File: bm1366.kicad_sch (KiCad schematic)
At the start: 47 parts, among them U12 BM1366_mode1, U5 MCP1824T-1202E/OT, U6 MCP1824T-0802E, U7 25MHz, U9 SN74AVC4T774

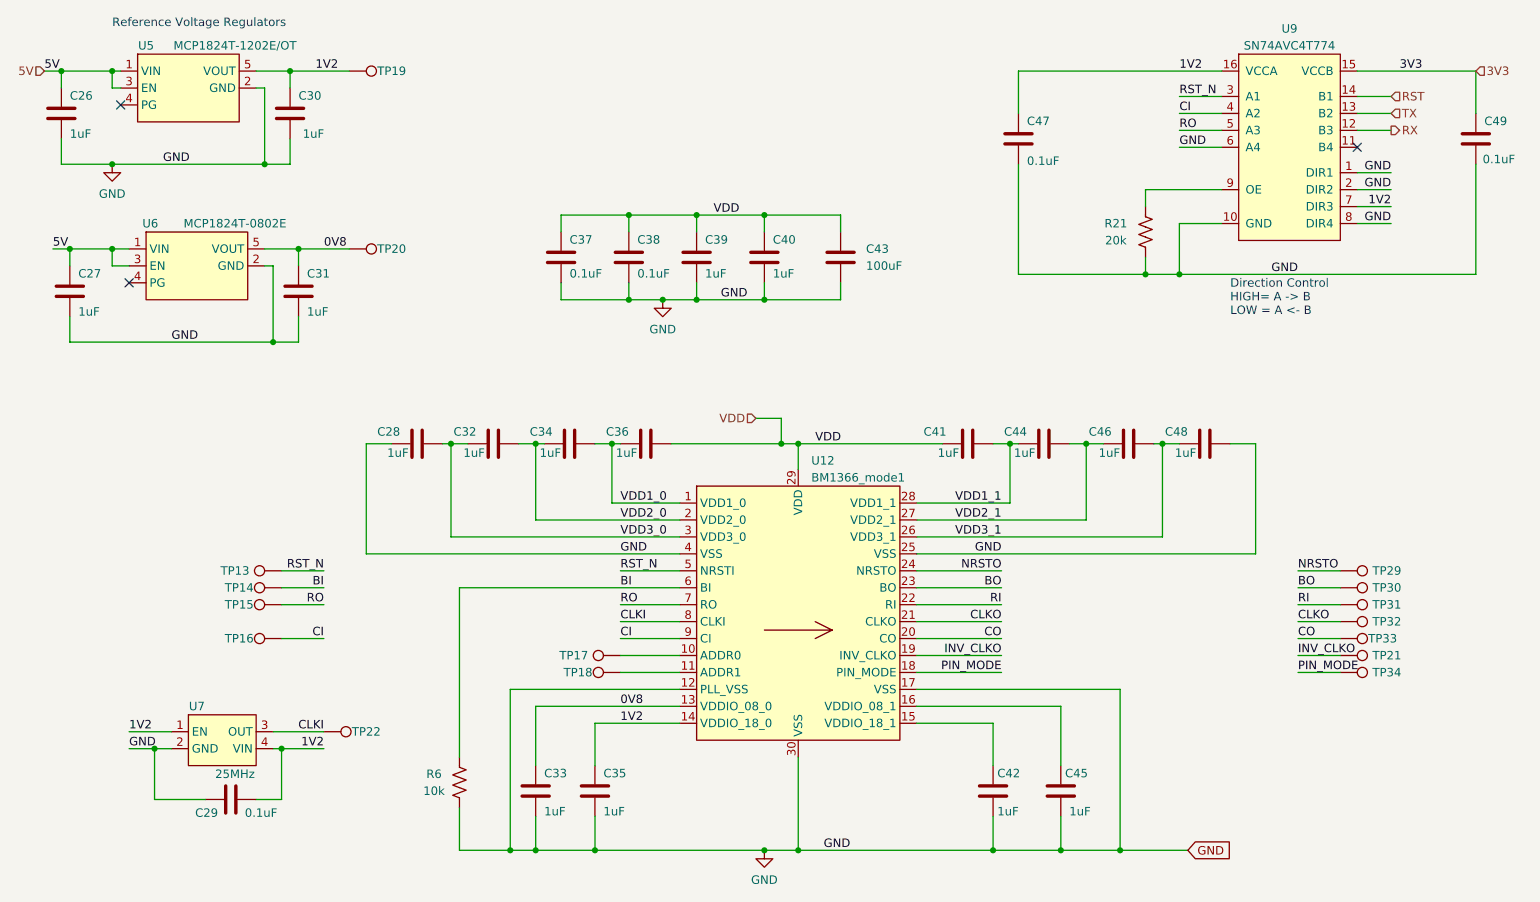
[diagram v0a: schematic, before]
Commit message: use global GND level provided by default with KiCad and remove custom global GND
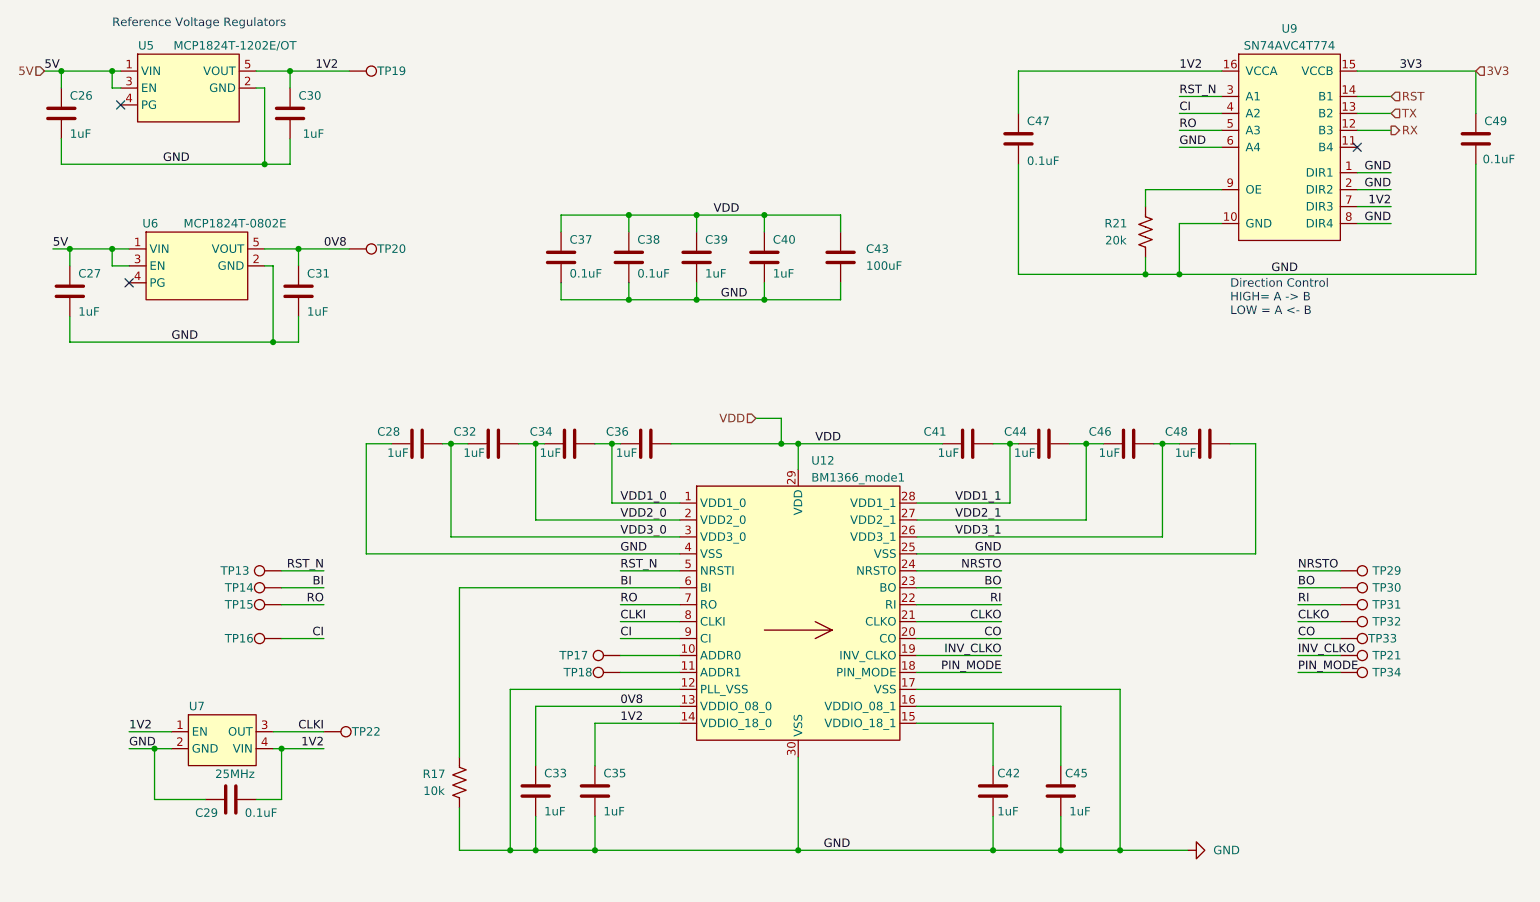
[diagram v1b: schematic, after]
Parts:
- renumbered R6 to R17
